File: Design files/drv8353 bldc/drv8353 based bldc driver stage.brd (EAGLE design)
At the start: 127 x 127 mm, 80 parts, among them IC1 DRV8350RSRGZT, J3 2X6 FEMALE, J4 B06B-HCMKK

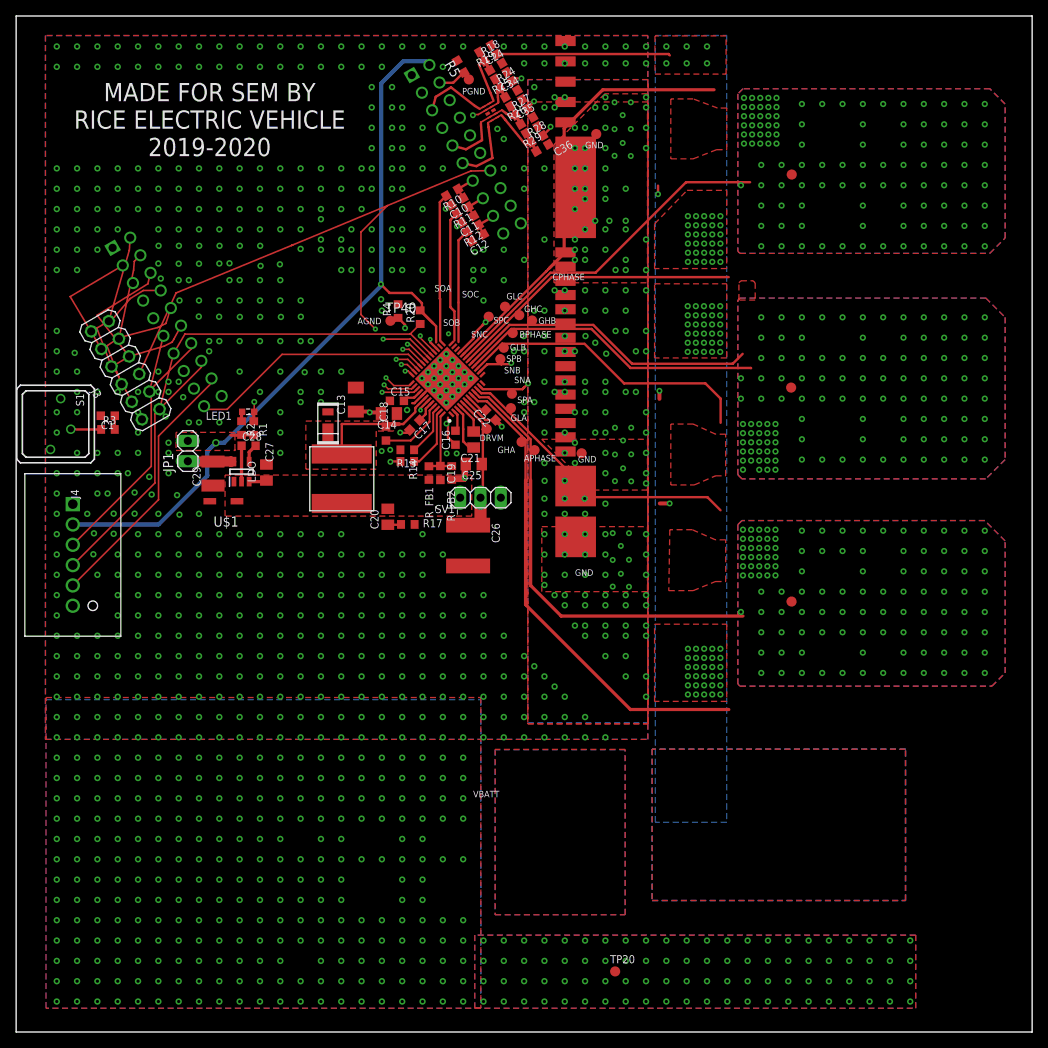
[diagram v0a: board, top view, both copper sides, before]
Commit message: reworked driver stage to work with board interface
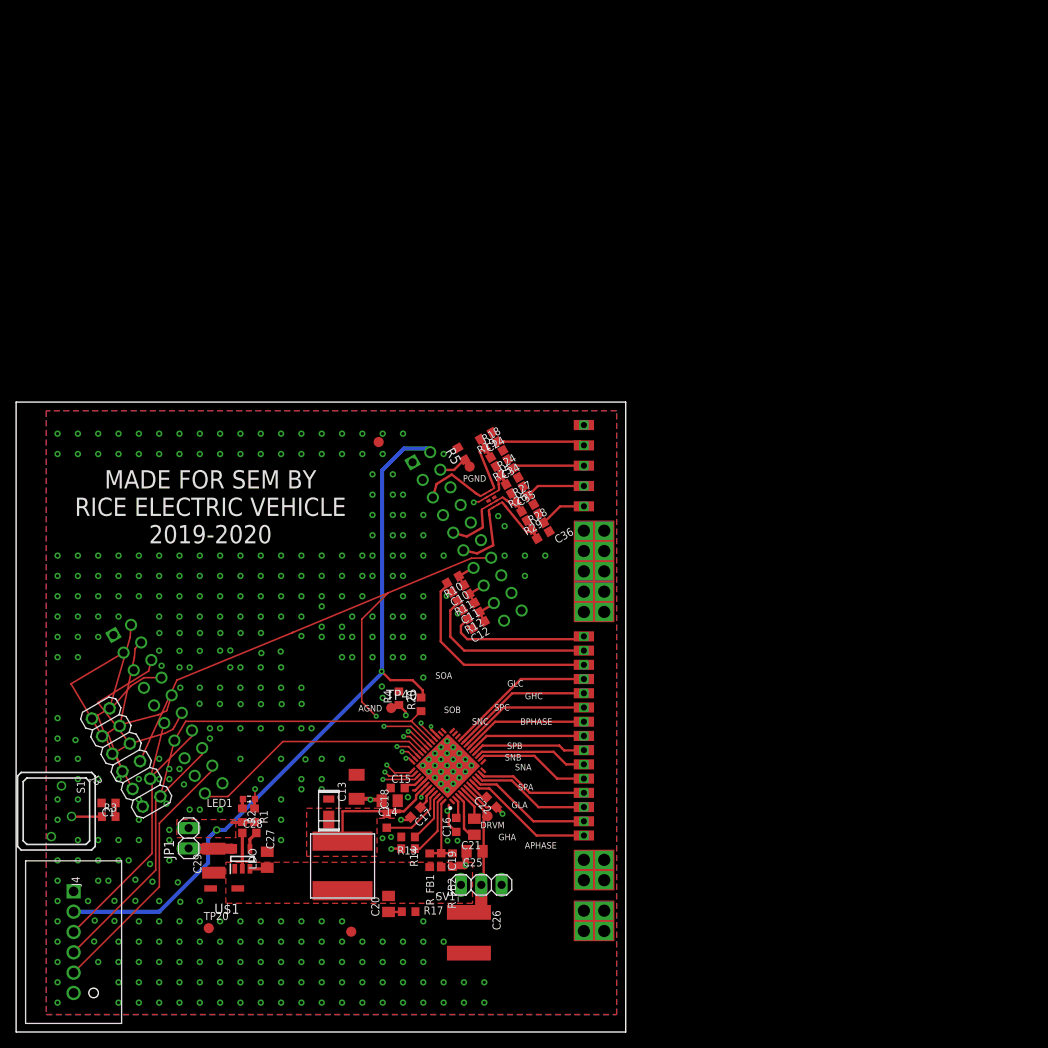
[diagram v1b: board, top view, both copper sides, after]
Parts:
- removed TP10, TP11, TP12, TP17, TP21, TP22, TP32, TP33, TP34, TP36, TP5, TP6, TP7, TP8, TP9: TPB1,27, testpad:B1,27
- U$3: value POWER_STAGE_CONNECTOR -> DRIVER_STAGE_CONNECTORDRIVER; device REV BLDC:POWER_STAGE_CONNECTION -> REV BLDC:DRIVER_STAGE_CONNECTION
- moved TP28 66.4 mm to (41.9, 12.5)
- moved TP20 51.1 mm to (24.1, 13.0)
- moved C1 48.4 mm to (11.6, 28.6)
- moved C11 48.4 mm to (56.5, 53.2)
- moved C12 48.4 mm to (57.8, 50.9)
- moved C14 48.4 mm to (46.7, 28.9)
- moved C15 48.4 mm to (47.7, 30.5)
- moved C17 48.4 mm to (49.9, 27.5)
- moved C21 48.4 mm to (57.3, 25.7)
- moved C22 48.4 mm to (59.4, 28.7)
- moved C24 48.4 mm to (60.1, 72.3)
- moved C27 48.4 mm to (31.4, 21.5)
- moved IC1 48.4 mm to (54.0, 33.2)
- moved J4 48.4 mm to (7.18, 17.6)
- moved JP1 48.4 mm to (21.6, 24.2)
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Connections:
- net 5V: now also U$3.5V, U$3.5VH
- net APHASE: now also U$3.APHASE, U$3.APHASE2, U$3.APHASE2H, U$3.APHASEH; no longer TP17.TP, TP32.TP
- net BPHASE: now also U$3.BPHASE, U$3.BPHASE2, U$3.BPHASE2H, U$3.BPHASEH; no longer TP21.TP, TP6.TP
- net CPHASE: now also U$3.CPHASE, U$3.CPHASE2, U$3.CPHASE2H, U$3.CPHASEH; no longer TP12.TP, TP22.TP
- net GHA: now also U$3.GHA, U$3.GHAH; no longer TP36.TP
- net GHB: now also U$3.GHB, U$3.GHBH; no longer TP8.TP
- net GHC: now also U$3.GHC, U$3.GHCH; no longer TP9.TP
- net GLA: now also U$3.GLA, U$3.GLAH; no longer TP33.TP
- net GLB: now also U$3.GLB, U$3.GLBH; no longer TP7.TP
- net GLC: now also U$3.GLC, U$3.GLCH; no longer TP11.TP
- net GND: now also U$3.GND, U$3.GND2, U$3.GND2H1, U$3.GND2H10, U$3.GND2H2, U$3.GND2H3, U$3.GND2H4, U$3.GND2H5, U$3.GND2H6, U$3.GND2H7, U$3.GND2H8, U$3.GND2H9, U$3.GNDH1, U$3.GNDH2, U$3.GNDH3, U$3.GNDH4
- net SLA: now also U$3.SLA, U$3.SLAH; no longer TP34.TP
- net SLB: now also U$3.SLB, U$3.SLBH; no longer TP5.TP
- net SLC: now also U$3.SLC, U$3.SLCH; no longer TP10.TP
- net SOA: now also U$3.SOA, U$3.SOAH
- net SOB: now also U$3.SOB, U$3.SOBH
- net SOC: now also U$3.SOC, U$3.SOCH
- net VDRAIN: now also U$3.VDRAIN, U$3.VDRAIN2, U$3.VDRAIN2H, U$3.VDRAINH1, U$3.VDRAINH2, U$3.VDRAINH3, U$3.VDRAINH4
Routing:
- net APHASE: track 177.7 -> 25.4 mm, vias 115 -> 0
- net BPHASE: track 129.6 -> 21.7 mm, vias 113 -> 0
- net CPHASE: track 73.7 -> 22.5 mm, vias 110 -> 0
- net GHA: track 61.5 -> 16.8 mm
- net GLC: track 54.8 -> 17.6 mm
- net 5V: track 0.00 -> 24.9 mm
- net GLB: track 38.8 -> 14.2 mm
- net GHB: track 39.0 -> 14.7 mm
- net GLA: track 37.8 -> 14.9 mm
- net GHC: track 37.9 -> 15.7 mm
- net SLA: track 34.9 -> 13.9 mm, vias 2 -> 0
- net SLC: track 36.5 -> 18.5 mm, vias 2 -> 0
- net SLB: track 26.1 -> 14.3 mm, vias 2 -> 0
- net SOA: track 18.5 -> 26.7 mm
- net 3V3: track 103.0 -> 95.9 mm
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- removed copper zone on layer 1, net APHASE
- removed copper zone on layer 15, net APHASE
- removed copper zone on layer 16, net APHASE
- removed copper zone on layer 2, net APHASE
- removed copper zone on layer 1, net BPHASE
- removed copper zone on layer 15, net BPHASE
- removed copper zone on layer 16, net BPHASE
- removed copper zone on layer 2, net BPHASE
- removed copper zone on layer 1, net CPHASE
- removed copper zone on layer 15, net CPHASE
- removed copper zone on layer 16, net CPHASE
- removed copper zone on layer 2, net CPHASE
- removed copper zone on layer 1, net N$15
- removed copper zone on layer 15, net N$15
- removed copper zone on layer 16, net N$15
- removed copper zone on layer 2, net N$15
- removed copper zone on layer 1, net SLA
- removed copper zone on layer 1, net SLB
- removed copper zone on layer 1, net SLC
- removed copper zone on layer 1, net VDRAIN
- removed copper zone on layer 16, net VDRAIN
- removed copper zone on layer 2, net VDRAIN
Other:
- board size 127 x 127 mm -> 76.2 x 78.7 mm
- board text removed: "CPHASE"
- board text removed: "GHB"
- board text removed: "GLB"
- board text removed: "GND"
- board text removed: "SOC"
- board text removed: "VBATT"
